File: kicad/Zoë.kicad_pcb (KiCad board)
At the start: 4 copper layers, 55 x 35 mm, 42 parts, among them X2Y-CAN 4.7nF X2Y, X2Y-RS485 4.7nF X2Y

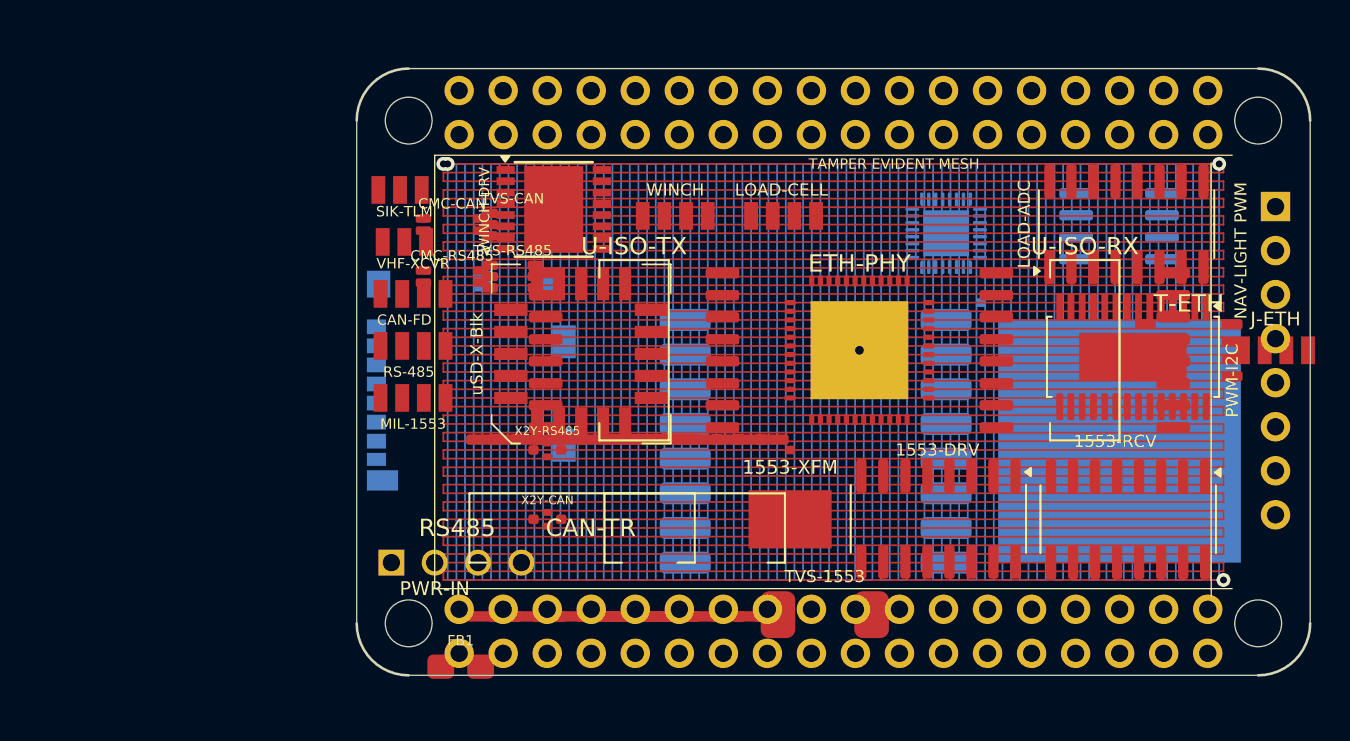
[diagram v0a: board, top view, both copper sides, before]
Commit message: avionics: wire second Ethernet (ETH2) on Wash; preserve Wash/Zoë layout work
Wash cape now carries a fully-wired second Ethernet channel.  The newly
placed ETH2 / ETH2-PHY (ADIN1300) / T-ETH2 (749010012A) footprints were
unconnected; this assigns their nets to mirror the ETH1 topology exactly:

  ETH2 (JST-GH-4P) --ETH2_LINE_{TX,RX}{P,N}--> T-ETH2 --ETH2_{TX,RX}{P,N}-->
  ETH2-PHY, reusing the host-side nets already broken out on the PB2-P2
  header (RMII1_* bus, shared MDIO/MDC, PHY2_INTRN/PHY2_RSTN, VCC2_ETH/
  GND/GND2_ETH).  44 pads assigned across the three parts (ETH2-PHY 32,
  T-ETH2 8, ETH2 4); diff-pair chains verified end to end.

Also preserves the manual component rearrangements on Wash and Zoë
(components reseated clear of the isolation moats).

Known follow-up (not in this commit): both PHYs share MDIO with no
address-strap resistors on the board (same default MDIO address); the
tamper-mesh shorts, ratsnest routing, and remaining DRC violations on all
four capes are still open.

Co-Authored-By: Claude Opus 4.8 <noreply@anthropic.com>
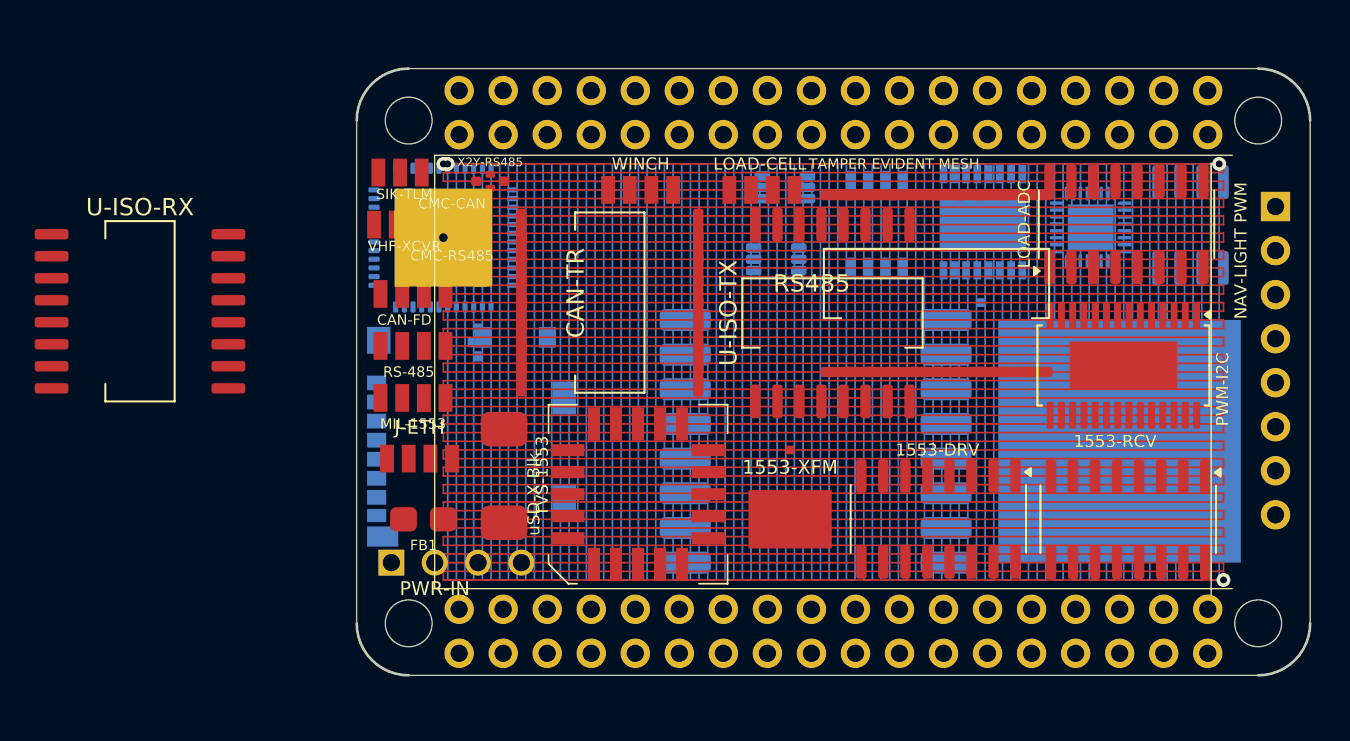
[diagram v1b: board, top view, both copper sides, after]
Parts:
- ETH-PHY, T-ETH, TVS-CAN, TVS-RS485, X2Y-CAN: moved to B.Cu
- WINCH DRV: moved to B.Cu
- moved U-ISO-RX 54.5 mm to (108.5, 101.5)
- moved J-ETH 49.8 mm to (124.6, 110.0)
- moved ETH-PHY 24.9 mm to (126.0, 97.2), turned to 180 degrees
- moved RS485 24.8 mm to (154.4, 99.9)
- moved WINCH DRV 24.8 mm to (157.1, 96.4), turned to 90 degrees
- moved TVS-1553 20.2 mm to (129.5, 111.0), turned to -90 degrees
- moved T-ETH 19.4 mm to (151.0, 96.5), turned to -90 degrees
- moved X2Y-RS485 15.8 mm to (128.7, 94.0)
- moved TVS-CAN 15.8 mm to (145.7, 94.3), turned to 180 degrees
- moved TVS-RS485 15.2 mm to (145.2, 98.5), turned to 180 degrees
- moved CAN-TR 13.9 mm to (135.6, 101.0), turned to 0 degrees
- moved U-ISO-TX 11.6 mm to (148.4, 101.6), turned to 90 degrees
- moved X2Y-CAN 11.0 mm to (128.0, 103.3), turned to -90 degrees
- moved FB1 8.77 mm to (124.8, 113.5), turned to 180 degrees
- moved uSD-X-Blk 8.73 mm to (137.2, 112.1)
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
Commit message: avionics: make Emma a stacking cape (P1/P2 + ETH + LoRa); Zoë passthrough rails
Implements the Rev R1 stack PocketBeagle -> Zoë -> Emma:

Emma (XCVR-49MHZ-2):
  * + PB2-P1/PB2-P2 2x18 sockets, wired pin-for-pin to the same nets as
    Zoë's headers (pass-through), making Emma a proper stacking cape.
  * + LoRa (RFM95W) moved from Zoë; wired to SPI1 (MISO/MOSI/CLK/CS_LORA)
    + LORA_RESETN, reached through the stack.
  * + Ethernet subsystem: ETH-PHY (ADIN1300) on RMII1 + PHY2_RSTN/INTRN
    (independent of Zoë's RMII0/PHY1), T-ETH (749010012A) and J-ETH on
    new EMMA_ETH_* MDI / EMMA_ETH_LINE_* nets. One ETH on Zoë, one on Emma.

Zoë:
  * - LoRa (now on Emma).
  * + PB2-P1-TOP / PB2-P2-TOP passthrough socket rails on the upper face,
    wired to the bottom-socket nets, so Emma stacks on top.

Net/component design only — new parts are placed at rough front-side
locations; dense 55x35 4-layer/both-side placement and routing are GUI
work (placement intentionally left for layout). LoRa 915 MHz antenna
routing on Emma and the now-redundant CAPE-B IF connector are follow-ups.

Co-Authored-By: Claude Opus 4.8 <noreply@anthropic.com>
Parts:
- removed LoRa: RFM95W, HOPERF_RFM9XW_SMD
- added PB2-P1-TOP: PB2I-P1-2x18, 2x18_P1_Socket, F.Cu at (148.5, 90.0)
- added PB2-P2-TOP: PB2I-P2-2x18, 2x18_P2_Socket, F.Cu at (148.5, 120.0)
